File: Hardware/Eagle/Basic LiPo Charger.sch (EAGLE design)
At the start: 10 parts, among them J1 USB-CON-5PIN-105017-0001, U1 MCP73831

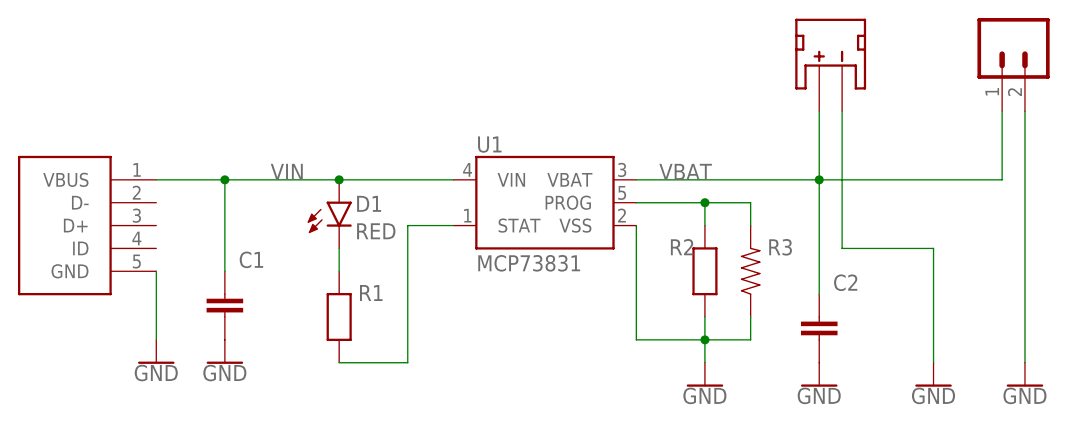
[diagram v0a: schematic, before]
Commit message: Changed resistor value
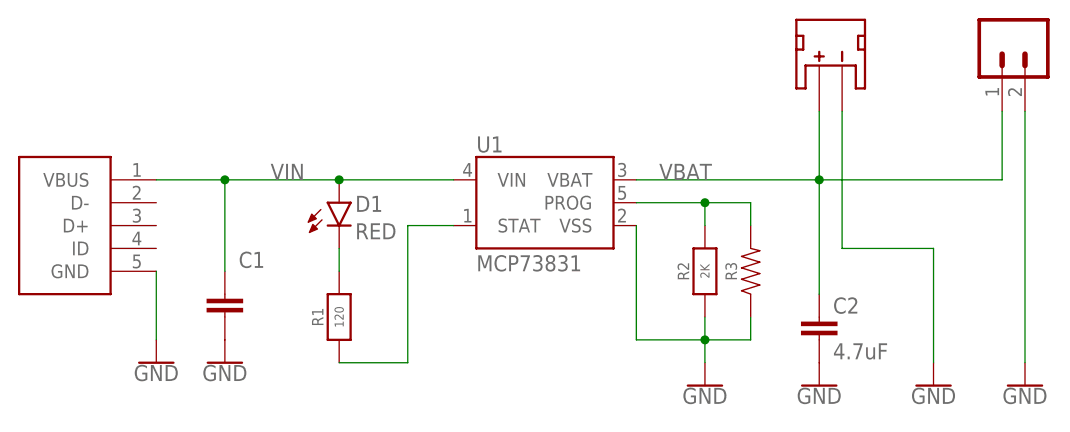
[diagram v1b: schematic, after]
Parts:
- R1: value 470 -> 120
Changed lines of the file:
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@@
 <?xml version="1.0" encoding="utf-8"?>
 <!DOCTYPE eagle SYSTEM "eagle.dtd">
-<eagle version="8.1.1">
+<eagle version="8.2.0">
 <drawing>
 <settings>
@@
 <part name="C1" library="NovemberFive-Basic" deviceset="CAPACITOR" device="" value="4.7uF"/>
 <part name="C2" library="NovemberFive-Basic" deviceset="CAPACITOR" device="" value="4.7uF"/>
-<part name="R1" library="NovemberFive-Basic" deviceset="RESISTOR" device="" value="470"/>
+<part name="R1" library="NovemberFive-Basic" deviceset="RESISTOR" device="" value="120"/>
 <part name="R2" library="NovemberFive-Basic" deviceset="RESISTOR" device="" value="2K"/>
 <part name="D1" library="SparkFun-LED" deviceset="LED-RED" device="0603" value="RED"/>
@@
 <attribute name="NAME" x="19.304" y="41.021" size="1.778" layer="95" font="vector"/>
 </instance>
-<instance part="C2" gate="G$1" x="83.82" y="35.56" smashed="yes">
-<attribute name="NAME" x="85.344" y="38.481" size="1.778" layer="95" font="vector"/>
-</instance>
-<instance part="R1" gate="G$1" x="30.48" y="35.56" smashed="yes" rot="R90">
-<attribute name="NAME" x="34.036" y="39.116" size="1.778" layer="95" font="vector" rot="R180" align="bottom-center"/>
-</instance>
-<instance part="R2" gate="G$1" x="71.12" y="40.64" smashed="yes" rot="R90">
-<attribute name="NAME" x="68.58" y="44.196" size="1.778" layer="95" font="vector" rot="R180" align="bottom-center"/>
-</instance>
+<instance part="C2" gate="G$1" x="83.82" y="35.56"/>
+<instance part="R1" gate="G$1" x="30.48" y="35.56" rot="R90"/>
+<instance part="R2" gate="G$1" x="71.12" y="40.64" rot="R90"/>
 <instance part="D1" gate="G$1" x="30.48" y="48.26" smashed="yes">
 <attribute name="NAME" x="32.258" y="47.244" size="1.778" layer="95" font="vector"/>
@@
 </instance>
 <instance part="R3" gate="G$1" x="76.2" y="40.64" smashed="yes" rot="R90">
-<attribute name="NAME" x="79.502" y="42.418" size="1.778" layer="95" font="vector" align="bottom-center"/>
+<attribute name="NAME" x="74.676" y="40.64" size="1.27" layer="95" font="vector" rot="R90" align="bottom-center"/>
 <attribute name="VALUE" x="77.724" y="40.64" size="1.778" layer="96" font="vector" rot="R90" align="top-center"/>
 </instance>
